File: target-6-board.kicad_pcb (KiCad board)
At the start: 2 copper layers, 99.1 x 90.7 mm, 55 parts, among them J1 Conn_01x10_Socket, J10 RJ14, J11 RJ14, J12 RJ14, J13 RJ14, J14 USB_A, J15 USB_A, J16 USB_C_Receptacle_PowerOnly_6P, J2 Conn_01x12_Socket, J3 Conn_01x10_Socket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

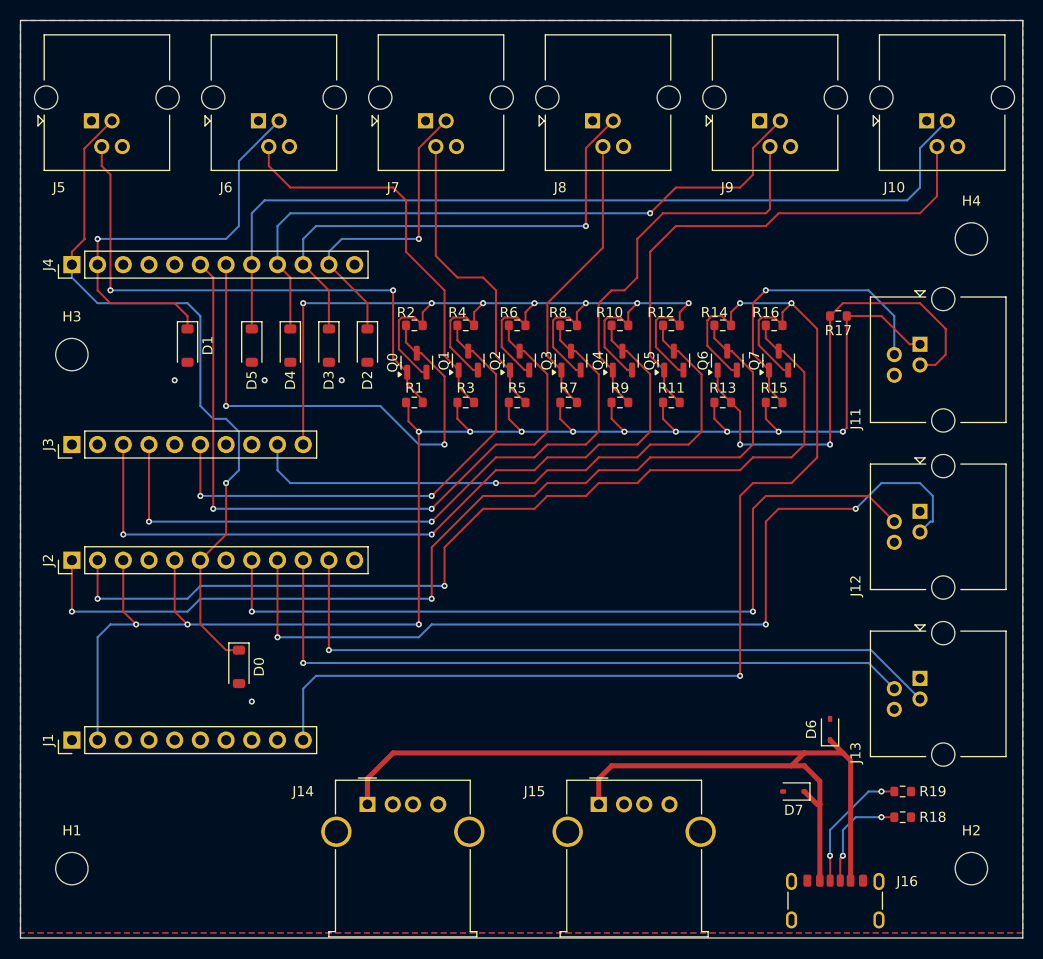
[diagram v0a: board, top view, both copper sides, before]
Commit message: fix NMOS type to BSS138 and PCB design
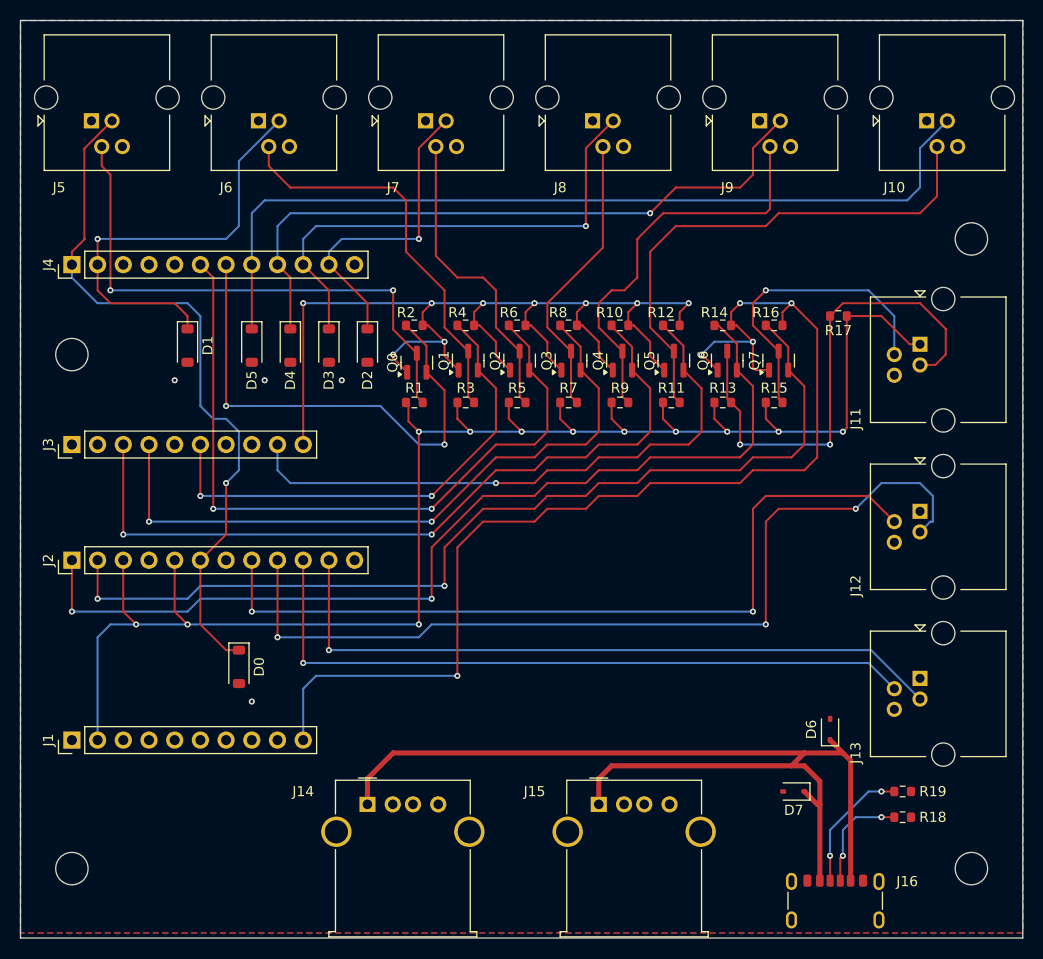
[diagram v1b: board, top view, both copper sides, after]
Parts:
- Q0, Q1, Q2, Q3, Q4, Q5, Q6, Q7: value NMOS -> Transistor_FET:BSS138
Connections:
- Q0 pad 1: TARGET_LED0 -> S0_VCC3V3
- Q0 pad 2: S0_VCC3V3 -> S0_GPIO8
- Q0 pad 3: S0_GPIO8 -> TARGET_LED0
- Q1 pad 1: TARGET_LED1 -> S0_VCC3V3
- Q1 pad 2: S0_VCC3V3 -> S0_GPIO9
- Q1 pad 3: S0_GPIO9 -> TARGET_LED1
- Q2 pad 1: TARGET_LED2 -> S0_VCC3V3
- Q2 pad 2: S0_VCC3V3 -> S0_GPIO10
- Q2 pad 3: S0_GPIO10 -> TARGET_LED2
- Q3 pad 1: TARGET_LED3 -> S0_VCC3V3
- Q3 pad 2: S0_VCC3V3 -> S0_GPIO18
- Q3 pad 3: S0_GPIO18 -> TARGET_LED3
- Q4 pad 1: TARGET_LED4 -> S0_VCC3V3
- Q4 pad 2: S0_VCC3V3 -> S0_GPIO19
- Q4 pad 3: S0_GPIO19 -> TARGET_LED4
- Q5 pad 1: TARGET_LED5 -> S0_VCC3V3
- Q5 pad 2: S0_VCC3V3 -> S0_GPIO21
- Q5 pad 3: S0_GPIO21 -> TARGET_LED5
- Q6 pad 1: SWITCH_BUTTON -> C_VCC3V3
- Q6 pad 2: C_VCC3V3 -> C_GPIO0
- Q6 pad 3: C_GPIO0 -> SWITCH_BUTTON
- Q7 pad 1: SWITCH_BUZZER -> C_VCC3V3
- Q7 pad 2: C_VCC3V3 -> C_GPIO1
- Q7 pad 3: C_GPIO1 -> SWITCH_BUZZER
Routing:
- net S0_VCC3V3: track 122.2 -> 106.0 mm, vias 7 -> 9
- net C_VCC3V3: track 120.8 -> 114.2 mm, vias 3 -> 5
- net SWITCH_BUTTON: track 48.4 -> 49.9 mm
- net S0_GPIO9: track 49.3 -> 48.6 mm
- net S0_GPIO8: track 50.8 -> 50.1 mm
- net S0_GPIO18: track 68.1 -> 67.4 mm
- net S0_GPIO10: track 73.2 -> 72.5 mm
